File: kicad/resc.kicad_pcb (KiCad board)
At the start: 4 copper layers, 51 x 75 mm, 168 parts, among them J1 CAN, J10 Conn_Coaxial, J2 HALL, J3 COMM, J4 POWER BTN, J5 SERVO, J6 SWD, J7 LED1, J8 LED2, J9 USB_C_Receptacle_USB2.0_14P, Q1 IRF7749L1, Q2 IRF7749L1, Q3 IRF7749L1, Q4 IRF7749L1, Q5 IRF7749L1, Q6 IRF7749L1, Q7 DMN62D0UW-7, SW1 SENSOR_VOLTAGE, U1 STM32F405RGTx, U10 AD8418, U11 SN74LVC1G66DCKR, U12 SN74LVC1G66DCKR, U13 SN74LVC1G66DCKR, U14 TC2117-3.3VDBTR, U15 USBLC6-2SC6, U16 NRF52832-QFAA-R, U2 TJA1051T-3, U3 SN74LVC1G66DCKR, U4 DRV8301DCAR, U5 SN74LVC1G66DCKR, U6 SN74LVC1G66DCKR, U7 BMI160, U8 AD8418, U9 AD8418, Y1 8MHz, Y2 32MHz

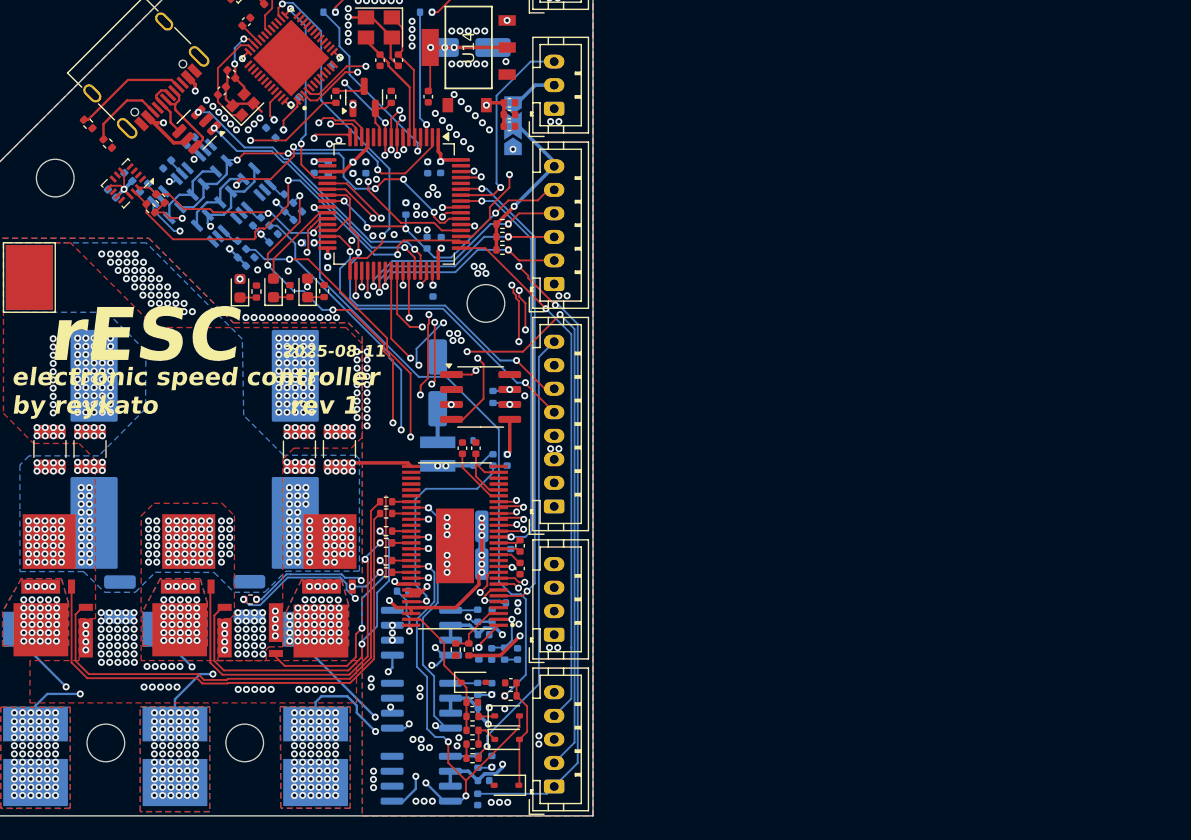
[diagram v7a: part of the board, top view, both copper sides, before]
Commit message: finalizing schematic for gate driver
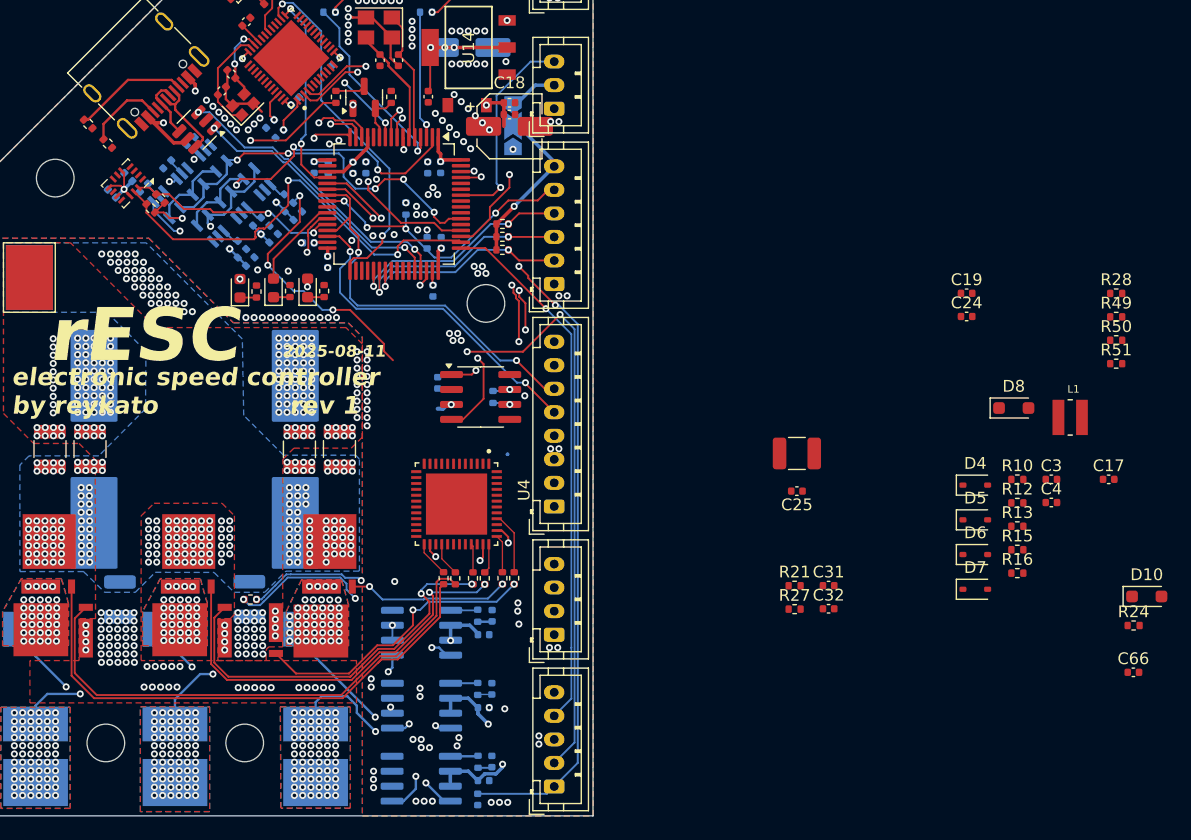
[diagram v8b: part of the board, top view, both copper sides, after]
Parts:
- removed C21: 100nF, Capacitor_SMD:C_0402_1005Metric
- removed C26: 22nF, Capacitor_SMD:C_0402_1005Metric
- removed C27, C28, C29: 220nF, Capacitor_SMD:C_0402_1005Metric
- removed C33: 15nF, Capacitor_SMD:C_0402_1005Metric
- removed C34: 2.2uF, Capacitor_SMD:C_0402_1005Metric
- removed R22: 18k, Resistor_SMD:R_0402_1005Metric
- removed R25: 10k, Resistor_SMD:R_0402_1005Metric
- added C66: 2.2uF, Capacitor_SMD:C_0402_1005Metric, F.Cu at (216.9, 107.8)
- added D10: D_Schottky, Diode_SMD:D_SOD-323_HandSoldering, F.Cu at (218.1, 101.3)
- added R49: 10k, Resistor_SMD:R_0402_1005Metric, F.Cu at (215.5, 77.6)
- added R50: 10k, Resistor_SMD:R_0402_1005Metric, F.Cu at (215.5, 79.6)
- added R51: 5.1k, Resistor_SMD:R_0402_1005Metric, F.Cu at (215.5, 81.6)
- C17, C23, C31, C32, L1, R27, R28: moved to F.Cu
- C18: value 2.2uF -> 47uF; footprint Capacitor_SMD:C_0402_1005Metric -> Capacitor_SMD:CP_Elec_5x5.3
- C19: value 2.2uF -> 1uF
- C20: value 100uF -> 1uF; footprint Capacitor_SMD:CP_Elec_5x5.4 -> Capacitor_SMD:C_0402_1005Metric
- C24: value 1uF -> 470nF 16V
- C25: value 4.7uF 100V -> 470nF 16V; footprint Capacitor_SMD:C_1210_3225Metric -> Capacitor_SMD:C_0402_1005Metric; moved to F.Cu
- C57: value 100uF -> 47uF
- D8: value ~ -> 3.6V; footprint Diode_SMD:D_SOD-323 -> Diode_SMD:D_SOD-323_HandSoldering; moved to F.Cu
- R21: value 220k -> 10k; moved to F.Cu
- R24: value 3.3k -> 0R
- U4: value DRV8301DCAR -> ~; footprint footprints:SOP50P810X120-57N -> footprints:QFN48P700X700X90
- moved R24 57.6 mm to (216.9, 103.8), turned to 0 degrees
- moved R28 55.7 mm to (215.5, 75.6), turned to 0 degrees
- moved L1 53.8 mm to (211.6, 86.1), turned to 0 degrees
- moved C3 52.7 mm to (209.9, 91.4)
- moved C17 51.1 mm to (214.8, 91.4), turned to 0 degrees
- moved R10 50.5 mm to (207.1, 91.4)
- moved R12 50.2 mm to (207.1, 93.4)
- moved R15 49.2 mm to (207.1, 97.4), turned to 0 degrees
- moved R16 48.9 mm to (207.1, 99.4), turned to 0 degrees
- moved C4 48.4 mm to (209.9, 93.4), turned to 0 degrees
- moved D8 46.1 mm to (206.8, 85.3), turned to 0 degrees
- moved R13 45.4 mm to (207.1, 95.4), turned to 0 degrees
- moved C19 44.8 mm to (202.8, 75.6), turned to 0 degrees
- moved D4 44.4 mm to (203.5, 91.9)
- moved D6 44.0 mm to (203.5, 97.8)
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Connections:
- C18 pad 1: +5V -> /Gate Driver/DRV_BUCK_OUT
- C19 pad 1: Net-(U4-DVDD) -> Net-(U4-VCCHS)
- C19 pad 2: GND -> /Gate Driver/SUPPLY
- C20 pad 1: +5V -> Net-(U4-VCCLS)
- C24 pad 1: Net-(U4-AVDD) -> Net-(U4-CP2L)
- C24 pad 2: GND -> Net-(U4-CP2H)
- C25 pad 1: SUPPLY -> Net-(U4-CP1L)
- C25 pad 2: GND -> Net-(U4-CP1H)
- C38 pad 1: SUPPLY -> /Gate Driver/SUPPLY
- C39 pad 1: SUPPLY -> /Gate Driver/SUPPLY
- C40 pad 1: SUPPLY -> /Gate Driver/SUPPLY
- C41 pad 1: SUPPLY -> /Gate Driver/SUPPLY
- C42 pad 1: SUPPLY -> /Gate Driver/SUPPLY
- C43 pad 1: SUPPLY -> /Gate Driver/SUPPLY
- C53 pad 1: SUPPLY -> /Gate Driver/SUPPLY
- C54 pad 1: SUPPLY -> /Gate Driver/SUPPLY
- D8 pad 2: GND -> Net-(D8-A)
- J9 pad A4: +5V -> Net-(J9-VBUS-PadA4)
- J9 pad A9: +5V -> Net-(J9-VBUS-PadA4)
- J9 pad B4: +5V -> Net-(J9-VBUS-PadA4)
- J9 pad B9: +5V -> Net-(J9-VBUS-PadA4)
- L1 pad 1: +5V -> /Gate Driver/DRV_BUCK_OUT
- L1 pad 2: Net-(D8-K) -> Net-(U4-PH)
- Q1 pad D: SUPPLY -> /Gate Driver/SUPPLY
- Q2 pad D: SUPPLY -> /Gate Driver/SUPPLY
- Q3 pad D: SUPPLY -> /Gate Driver/SUPPLY
- R21 pad 2: Net-(U4-RT_CLK) -> Net-(D8-K)
- R24 pad 1: Net-(U4-VSENSE) -> Net-(J9-VBUS-PadA4)
- R24 pad 2: GND -> Net-(D10-A)
- R43 pad 1: SUPPLY -> /Gate Driver/SUPPLY
- TP3 pad 1: SUPPLY -> /Gate Driver/SUPPLY
- U1 pad 53: /Gate Driver/SCLK -> /MCU/SPI3_SCK
- U1 pad 59: /Gate Driver/FAULT -> /MCU/FAULT
- U4 pad 1: Net-(U4-RT_CLK) -> /Gate Driver/CS
- U4 pad 10: /Gate Driver/SDO -> /Gate Driver/INH_C
- U4 pad 11: /Gate Driver/SCLK -> /Gate Driver/INL_C
- U4 pad 13: Net-(U4-GVDD) -> Net-(D8-K)
- U4 pad 14: Net-(U4-CP1) -> +5V
- U4 pad 15: Net-(U4-CP2) -> /Gate Driver/SUPPLY
- U4 pad 16: /Gate Driver/EN_GATE -> Net-(U4-PH)
- U4 pad 17: /Gate Driver/INH_A -> GND
- U4 pad 18: /Gate Driver/INL_A -> /Gate Driver/DRV_BUCK_OUT
- U4 pad 19: /Gate Driver/INH_B -> Net-(U4-CP1L)
- U4 pad 2: /Gate Driver/COMP -> /Gate Driver/SCK
- U4 pad 20: /Gate Driver/INL_B -> Net-(U4-CP1H)
- U4 pad 21: /Gate Driver/INH_C -> Net-(U4-CP2L)
- U4 pad 22: /Gate Driver/INL_C -> Net-(U4-CP2H)
- U4 pad 23: Net-(U4-DVDD) -> Net-(U4-VCCLS)
- U4 pad 24: Net-(U4-AVDD) -> Net-(U4-VCCHS)
- U4 pad 25: unconnected-(U4-SO1-Pad25) -> /Gate Driver/GH_C
- U4 pad 26: unconnected-(U4-SO2-Pad26) -> /Gate Driver/SH_C
- U4 pad 27: Net-(U4-AVDD) -> (no net)
- U4 pad 28: GND -> /Gate Driver/GL_C
- U4 pad 29: SUPPLY -> GND
- U4 pad 3: Net-(U4-VSENSE) -> /Gate Driver/SDO
- U4 pad 33: GND -> /Gate Driver/GL_B
- U4 pad 34: GND -> (no net)
- U4 pad 35: /Gate Driver/GL_C -> /Gate Driver/SH_B
- U4 pad 36: /Gate Driver/SH_C -> /Gate Driver/GH_B
- U4 pad 37: /Gate Driver/GH_C -> /Gate Driver/GH_A
- U4 pad 38: /Gate Driver/BST_C -> /SH_A
- U4 pad 39: GND -> (no net)
- U4 pad 4: unconnected-(U4-PWRGD-Pad4) -> /Gate Driver/SDI
- U4 pad 40: /Gate Driver/GL_B -> /Gate Driver/GL_A
- U4 pad 41: /Gate Driver/SH_B -> GND
- U4 pad 42: /Gate Driver/GH_B -> GND
- U4 pad 43: /Gate Driver/BST_B -> unconnected-(U4-CSOA-Pad43)
- U4 pad 44: GND -> unconnected-(U4-CSOB-Pad44)
- U4 pad 45: /Gate Driver/GL_A -> unconnected-(U4-CSOC-Pad45)
- U4 pad 46: /SH_A -> unconnected-(U4-VREF-Pad46)
- U4 pad 47: /Gate Driver/GH_A -> /Gate Driver/DRV_CE
- U4 pad 48: /Gate Driver/BST_A -> /Gate Driver/EN_GATE
- U4 pad 49: VDD -> GND
- U4 pad 5: unconnected-(U4-~{OCTW}-Pad5) -> /Gate Driver/nFAULT
- U4 pad 6: /Gate Driver/FAULT -> /Gate Driver/INH_A
- U4 pad 7: Net-(U4-DTC) -> /Gate Driver/INL_A
- U4 pad 8: /Gate Driver/CS -> /Gate Driver/INH_B
- U4 pad 9: /Gate Driver/SDI -> /Gate Driver/INL_B
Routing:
- net /MCU/CURRENT_1: track 90.8 -> 29.6 mm, vias 4 -> 2
- net SUPPLY: track 58.5 -> 0.00 mm, vias 239 -> 0
- net /MCU/CURRENT_3: track 77.4 -> 22.9 mm, vias 5 -> 3
- net /SHUTDOWN: track 52.7 -> 0.00 mm, vias 2 -> 0
- net /MCU/CURRENT_2: track 76.0 -> 27.8 mm, vias 4 -> 2
- net /Gate Driver/FAULT: track 40.9 -> 0.00 mm, vias 2 -> 0
- net /Gate Driver/SDO: track 40.6 -> 0.00 mm, vias 4 -> 0
- net /Gate Driver/SDI: track 40.3 -> 0.00 mm, vias 4 -> 0
- net /CONN_SW: track 71.9 -> 33.8 mm, vias 2 -> 1
- net /Gate Driver/SCLK: track 37.0 -> 0.00 mm, vias 4 -> 0
- net /Gate Driver/EN_GATE: track 35.1 -> 0.00 mm, vias 2 -> 0
- net /Gate Driver/SH_B: track 71.4 -> 37.4 mm, vias 39 -> 37
- net /Gate Driver/CS: track 33.3 -> 0.00 mm, vias 2 -> 0
- net /SH_A: track 93.8 -> 60.9 mm, vias 52 -> 49
- net /Gate Driver/SH_C: track 93.3 -> 60.8 mm, vias 39 -> 37
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- added copper zone on B.Cu, net /Gate Driver/SUPPLY
- added copper zone on In2.Cu, net /Gate Driver/SUPPLY
- removed copper zone on B.Cu, net SUPPLY
- removed copper zone on In2.Cu, net SUPPLY
